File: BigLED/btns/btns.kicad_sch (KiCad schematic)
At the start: 12 parts, among them J1 Conn_01x05_Socket, SW1 TSX101G100-250, SW2 RotaryEncoder_Switch, SW3 SW_Push, SW4 SW_Push, SW5 SW_Push, SW6 SW_Push, SW7 SW_Push, SW8 SW_Push, U1 PY32F002AF15P6TU, U3 74LVC2G66

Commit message: Finist SCH for BigLED
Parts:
- removed U2: ~, symbol local:OLED
- added C1, C2, C3: 1.0, symbol Device:C
- added C4: NP, symbol Device:C
- added J2: Prog, symbol Connector:Conn_01x06_Pin
- added JP1: SolderJumper_3_Open, symbol Jumper:SolderJumper_3_Open
- added R1: 100K, symbol Device:R
- added SW9: SW_Push, symbol Switch:SW_Push
- added TP1, TP2: TestPoint, symbol Connector:TestPoint
- added U4: SSD1306 OLED, local:SDD1306, symbol locals:SSD1306
- J1: value Conn_01x05_Socket -> MainBrd
- SW1: symbol EasyEDA:TSX101G100-250 -> local:TSX101G100-250
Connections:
- net at SW1.1: now also U1.3 (PA14-SWC), SW9.1, TP2.1
- net B5: now reaches SW1.2 (←)
- net B5: now also SW7.2, U1.12 (PA1)
- net B4: now reaches SW1.3 (Hit)
- net B4: now also SW3.2, U1.15 (PA4)
- net B1: now reaches SW1.4 (↑)
- net B1: now also SW4.2, U1.18 (PB2)
- net B2: now reaches SW1.5 (→)
- net B2: now also SW5.2, U1.17 (PB0)
- net B3: now reaches SW1.6 (↓)
- net B3: now also SW6.2, U1.16 (PA7)
- net at U3.3: now also U1.19 (PB1), U3.7, R1.2
- net SDA: now reaches U3.5
- net SDA: now also J1.3 (Pin_3), U1.8 (PF0-OSCIN)
- net at U3.6: now also U4.4 (SDA)
- net at SW6.1: now also SW3.1, SW4.1, SW5.1, SW7.1, SW8.1, U1.2 (PA13-SWD), TP1.1
- net SCL: now reaches U3.1
- net SCL: now also J1.2 (Pin_2), U1.9 (PF1-OSCOUT)
- net at U3.2: now also U4.3 (SCL)
- net +3.3V: now reaches J1.1 (Pin_1)
- net +3.3V: now also SW2.C, SW2.S2, U1.20 (VCC), U3.8 (VCC), C1.2, C2.2, C3.1, J2.1 (Pin_1), JP1.1 (A), U4.2 (VCC)
- net GND: now reaches J1.4 (Pin_4)
- net GND: now also U1.1 (VSS), U3.4 (GND), C1.1, C2.1, C3.2, C4.1, J2.6 (Pin_6), JP1.3 (B), U4.1 (GND)
- net INT: now reaches J1.5 (Pin_5)
- net INT: now also U1.7 (PA5)
- net at SW2.A: now also U1.6 (PA6)
- net at SW2.B: now also U1.4 (PB3)
- net at SW2.S1: now also U1.5 (PB6/PF4-BOOT0), J2.2 (Pin_2)
- net at U1.10 (PF2-NRST): now also C4.2, J2.3 (Pin_3)
- net B6: now reaches U1.11 (PA0)
- net B6: now also SW8.2, SW9.2
- net at U1.13 (PA2): now also J2.4 (Pin_4)
- net at U1.14 (PA3): now also J2.5 (Pin_5)
- new net: JP1.2 (C), R1.1
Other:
- moved on the sheet: J1, SW2, U1, U3A, U3B, U3C

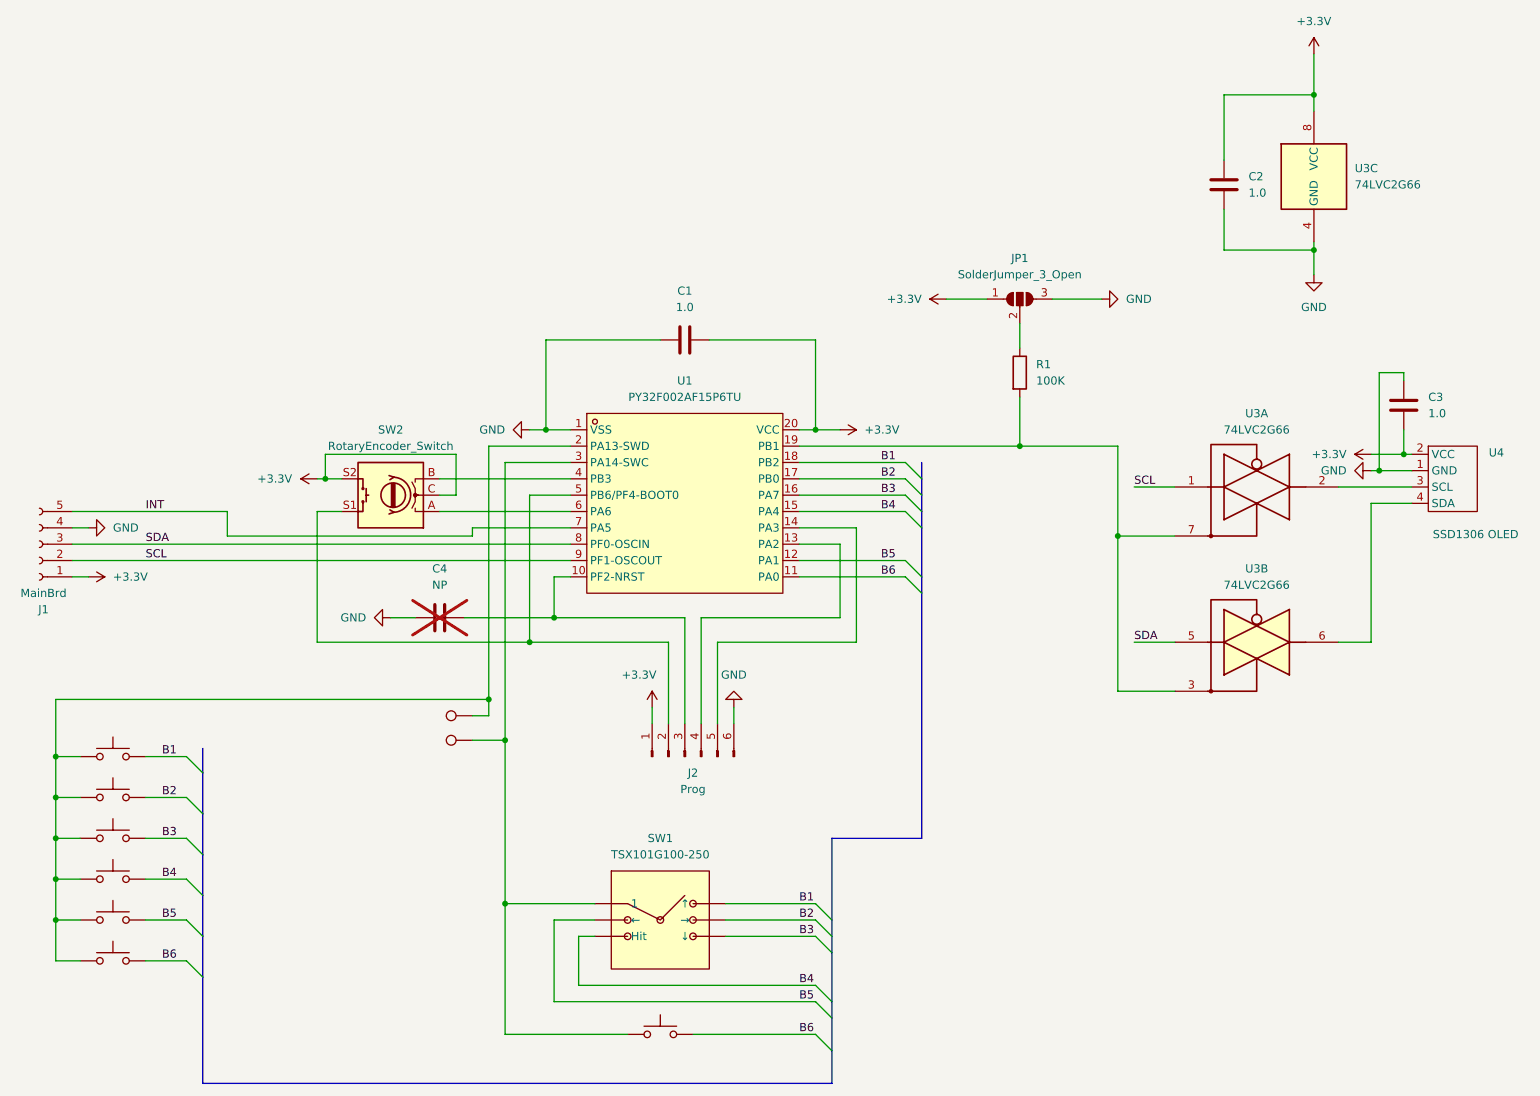
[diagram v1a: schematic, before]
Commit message: Converted BigLED to KiCAD v9
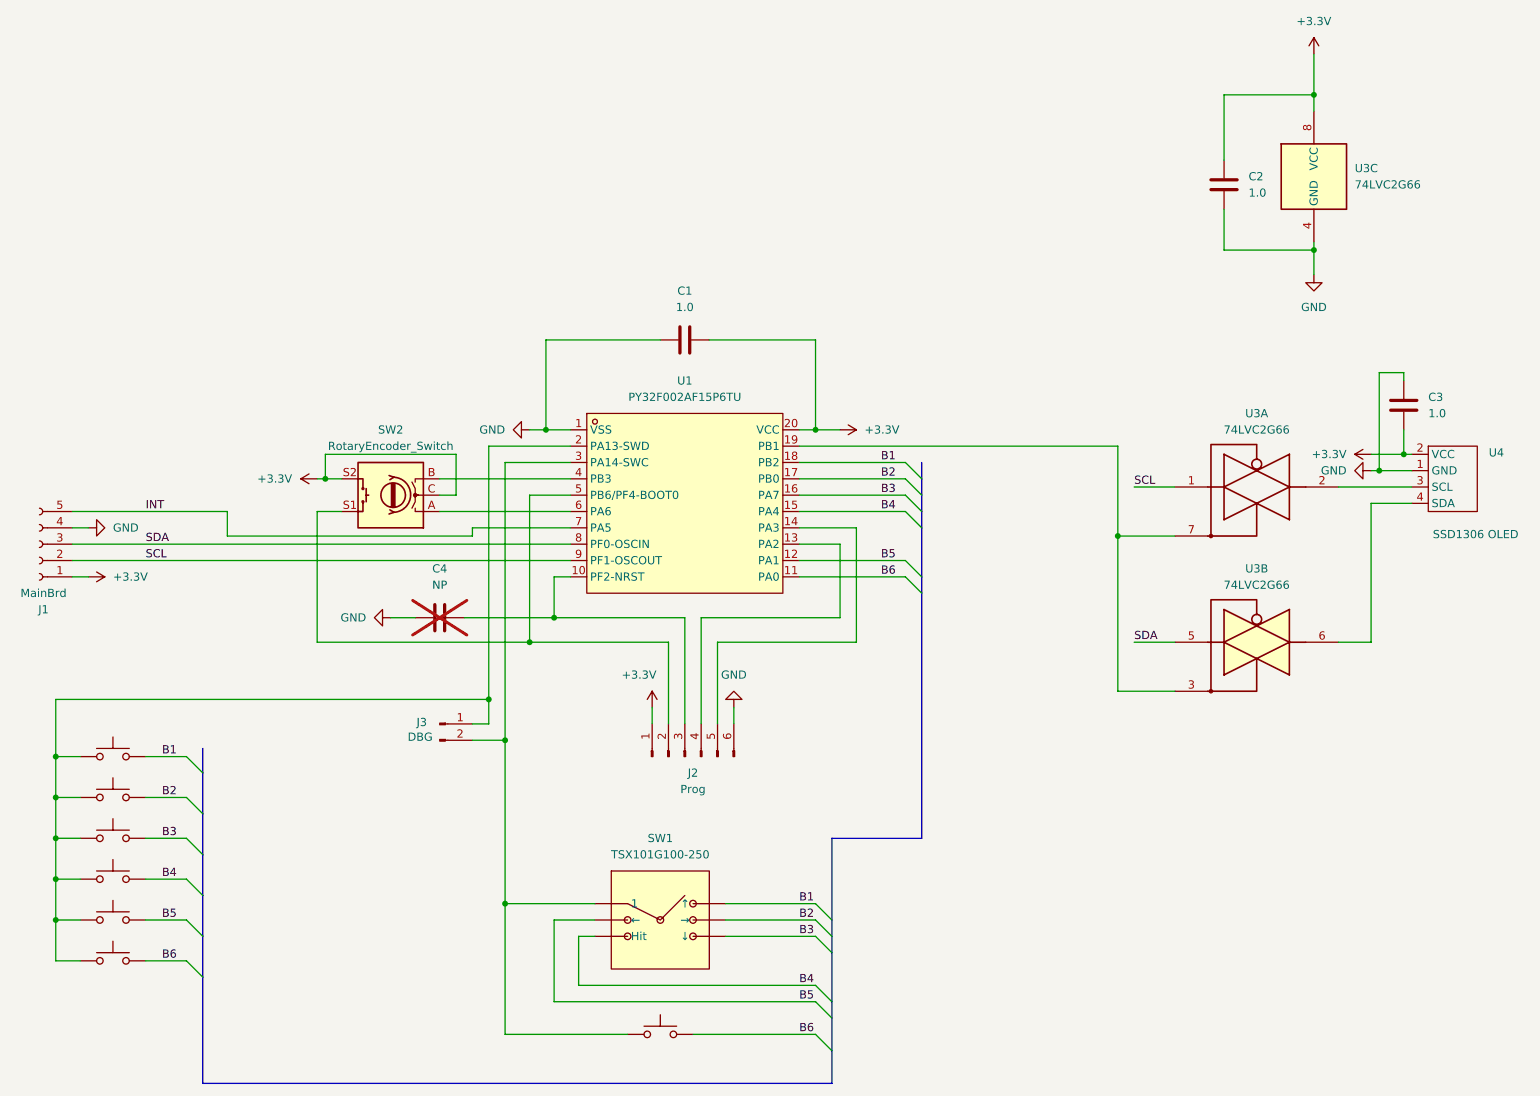
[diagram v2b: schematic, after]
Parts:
- removed JP1: SolderJumper_3_Open, symbol Jumper:SolderJumper_3_Open
- removed R1: 100K, symbol Device:R
- removed TP1, TP2: TestPoint, symbol Connector:TestPoint
- added J3: DBG, symbol Connector:Conn_01x02_Pin
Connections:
- net at SW1.1, SW9.1, U1.3 (PA14-SWC): now also J3.2 (Pin_2)
- net at SW3.1, SW4.1, SW5.1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: now also J3.1 (Pin_1)
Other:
- company: (none) -> RoboWay
- title: (none) -> BigLED (Buttons)

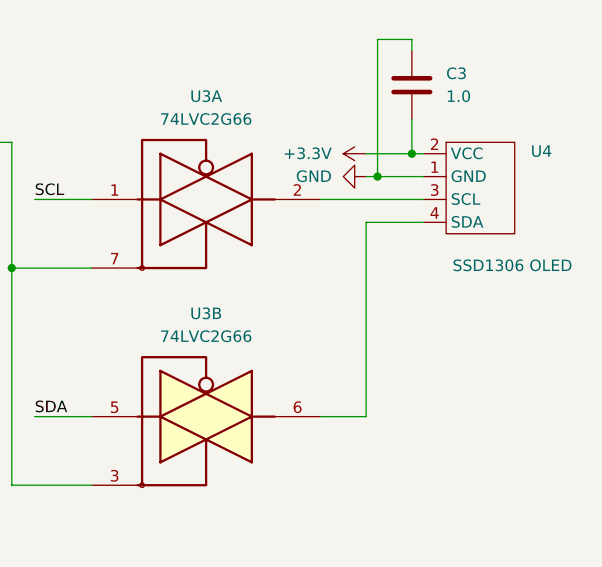
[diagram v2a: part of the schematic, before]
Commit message: Added dedicated pull ups for OLED display
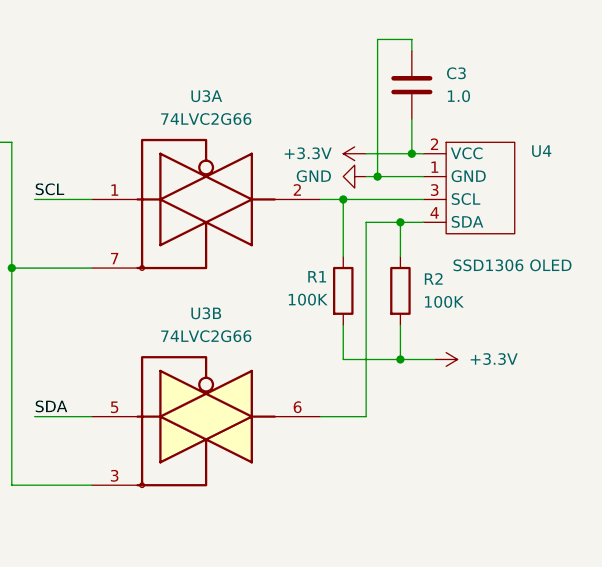
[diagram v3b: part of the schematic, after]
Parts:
- added R1, R2: 100K, symbol Device:R
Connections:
- net +3.3V: now also R1.2, R2.2
- net at U3.6, U4.4 (SDA): now also R2.1
- net at U3.2, U4.3 (SCL): now also R1.1

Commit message: Assigned packages for BigLED subprojects
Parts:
- C1, C2, C3, C4: footprint (none) -> Capacitor_SMD:C_0603_1608Metric_Pad1.08x0.95mm_HandSolder
- J1: footprint (none) -> Connector_JST:JST_XH_B5B-XH-A_1x05_P2.50mm_Vertical
- J2: footprint (none) -> Connector_PinHeader_2.54mm:PinHeader_2x03_P2.54mm_Vertical
- J3: footprint (none) -> Connector_PinHeader_2.54mm:PinHeader_1x02_P2.54mm_Vertical
- R1, R2: footprint (none) -> Resistor_SMD:R_0603_1608Metric_Pad0.98x0.95mm_HandSolder
- SW2: footprint (none) -> Rotary_Encoder:RotaryEncoder_Alps_EC11E-Switch_Vertical_H20mm
- SW3, SW4, SW5, SW6, SW7, SW8, SW9: footprint (none) -> local:KEY-TH_4P-L6.0-W6.0-P4.50-LS6.50
- U3: footprint (none) -> Package_SO:SSOP-8_2.95x2.8mm_P0.65mm
- U4: footprint local:SDD1306 -> easyeda2kicad:OLED-TH_L27.8-W27.2-P2.54_C9900033791
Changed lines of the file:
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@@
 			)
 		)
-		(property "Footprint" ""
+		(property "Footprint" "Package_SO:SSOP-8_2.95x2.8mm_P0.65mm"
 			(at 223.52 115.57 0)
 			(effects
@@
 			)
 		)
-		(property "Footprint" ""
+		(property "Footprint" "Capacitor_SMD:C_0603_1608Metric_Pad1.08x0.95mm_HandSolder"
 			(at 138.43 67.6148 0)
 			(effects
@@
 			)
 		)
-		(property "Footprint" ""
+		(property "Footprint" "local:KEY-TH_4P-L6.0-W6.0-P4.50-LS6.50"
 			(at 45.72 140.97 0)
 			(effects
@@
 			)
 		)
-		(property "Footprint" ""
+		(property "Footprint" "Package_SO:SSOP-8_2.95x2.8mm_P0.65mm"
 			(at 223.52 91.44 0)
 			(effects
@@
 			)
 		)
-		(property "Footprint" ""
+		(property "Footprint" "local:KEY-TH_4P-L6.0-W6.0-P4.50-LS6.50"
 			(at 130.81 171.45 0)
 			(effects
@@
 			)
 		)
-		(property "Footprint" ""
+		(property "Footprint" "Connector_PinHeader_2.54mm:PinHeader_1x02_P2.54mm_Vertical"
 			(at 96.52 128.27 0)
 			(effects
@@
 			)
 		)
-		(property "Footprint" ""
+		(property "Footprint" "local:KEY-TH_4P-L6.0-W6.0-P4.50-LS6.50"
 			(at 45.72 147.32 0)
 			(effects
@@
 			)
 		)
-		(property "Footprint" ""
+		(property "Footprint" "Capacitor_SMD:C_0603_1608Metric_Pad1.08x0.95mm_HandSolder"
 			(at 217.4748 40.64 0)
 			(effects
@@
 			)
 		)
-		(property "Footprint" ""
+		(property "Footprint" "Capacitor_SMD:C_0603_1608Metric_Pad1.08x0.95mm_HandSolder"
 			(at 100.33 110.7948 0)
 			(effects
@@
 			)
 		)
-		(property "Footprint" ""
+		(property "Footprint" "Connector_PinHeader_2.54mm:PinHeader_2x03_P2.54mm_Vertical"
 			(at 134.62 133.35 0)
 			(effects
@@
 			)
 		)
-		(property "Footprint" ""
+		(property "Footprint" "Connector_JST:JST_XH_B5B-XH-A_1x05_P2.50mm_Vertical"
 			(at 34.29 100.33 0)
 			(effects
@@
 			)
 		)
-		(property "Footprint" ""
+		(property "Footprint" "Capacitor_SMD:C_0603_1608Metric_Pad1.08x0.95mm_HandSolder"
 			(at 245.4148 74.93 0)
 			(effects
@@
 			)
 		)
-		(property "Footprint" ""
+		(property "Footprint" "local:KEY-TH_4P-L6.0-W6.0-P4.50-LS6.50"
 			(at 45.72 128.27 0)
 			(effects
@@
 			)
 		)
-		(property "Footprint" ""
+		(property "Footprint" "Package_SO:SSOP-8_2.95x2.8mm_P0.65mm"
 			(at 232.41 43.18 0)
 			(effects
@@
 			)
 		)
-		(property "Footprint" ""
+		(property "Footprint" "Rotary_Encoder:RotaryEncoder_Alps_EC11E-Switch_Vertical_H20mm"
 			(at 92.71 96.774 0)
 			(effects
@@
 			)
 		)
-		(property "Footprint" ""
+		(property "Footprint" "local:KEY-TH_4P-L6.0-W6.0-P4.50-LS6.50"
 			(at 45.72 153.67 0)
 			(effects
@@
 			)
 		)
-		(property "Footprint" ""
+		(property "Footprint" "local:KEY-TH_4P-L6.0-W6.0-P4.50-LS6.50"
 			(at 45.72 134.62 0)
 			(effects
@@
 			)
 		)
-		(property "Footprint" "local:SDD1306"
+		(property "Footprint" "easyeda2kicad:OLED-TH_L27.8-W27.2-P2.54_C9900033791"
 			(at 255.27 86.36 0)
 			(effects
@@
 			)
 		)
-		(property "Footprint" ""
+		(property "Footprint" "Resistor_SMD:R_0603_1608Metric_Pad0.98x0.95mm_HandSolder"
 			(at 243.332 101.6 90)
 			(effects
@@
 			)
 		)
-		(property "Footprint" ""
+		(property "Footprint" "local:KEY-TH_4P-L6.0-W6.0-P4.50-LS6.50"
 			(at 45.72 160.02 0)
 			(effects
@@
 			)
 		)
-		(property "Footprint" ""
+		(property "Footprint" "Resistor_SMD:R_0603_1608Metric_Pad0.98x0.95mm_HandSolder"
 			(at 236.982 101.6 90)
 			(effects

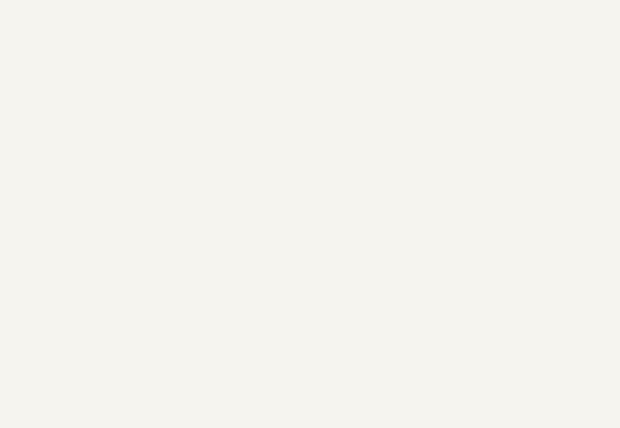
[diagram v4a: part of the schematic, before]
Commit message: PCB for BigLED Panel started
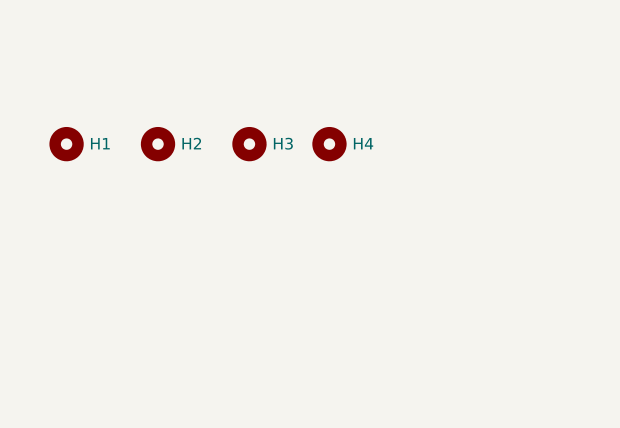
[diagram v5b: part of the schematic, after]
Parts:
- added H1, H2, H3, H4: MountingHole, MountingHole:MountingHole_3.2mm_M3, symbol Mechanical:MountingHole
